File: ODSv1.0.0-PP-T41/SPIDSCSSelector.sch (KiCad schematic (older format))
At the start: 4 parts, among them U1 MAX7317, U2 74HC4067PW

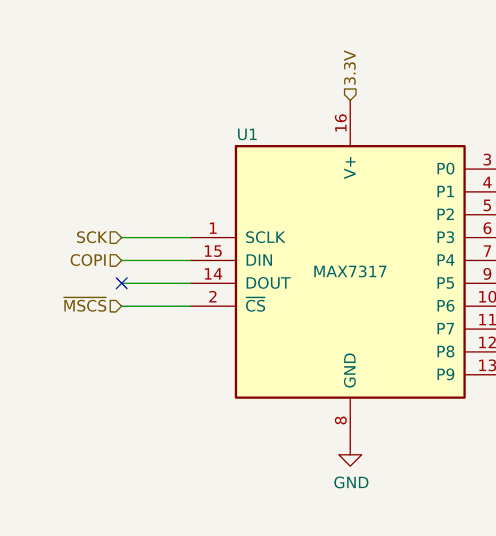
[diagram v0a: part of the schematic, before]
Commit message: Disconnect BT & BP-Jmp backbone MAX7317 DOUT (#16); make DOUT output pin
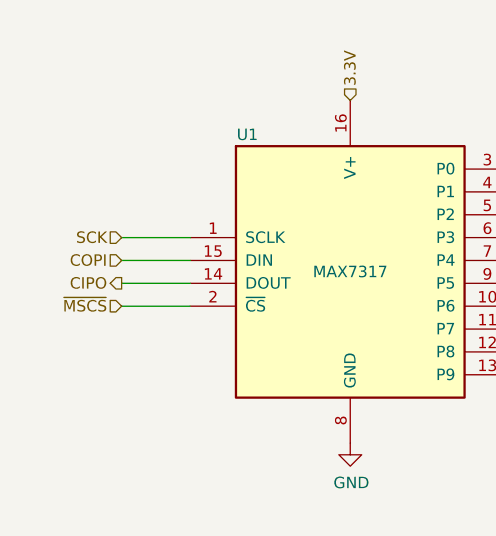
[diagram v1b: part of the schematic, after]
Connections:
- net CIPO: now reaches U1.14 (DOUT)
- no-connect marks 1 -> 0
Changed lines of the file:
@@
 	1    0    0    -1
 $EndComp
-NoConn ~ 1000 2150
+Text HLabel 1000 2150 0    50   Output ~ 0
+CIPO
 $EndSCHEMATC

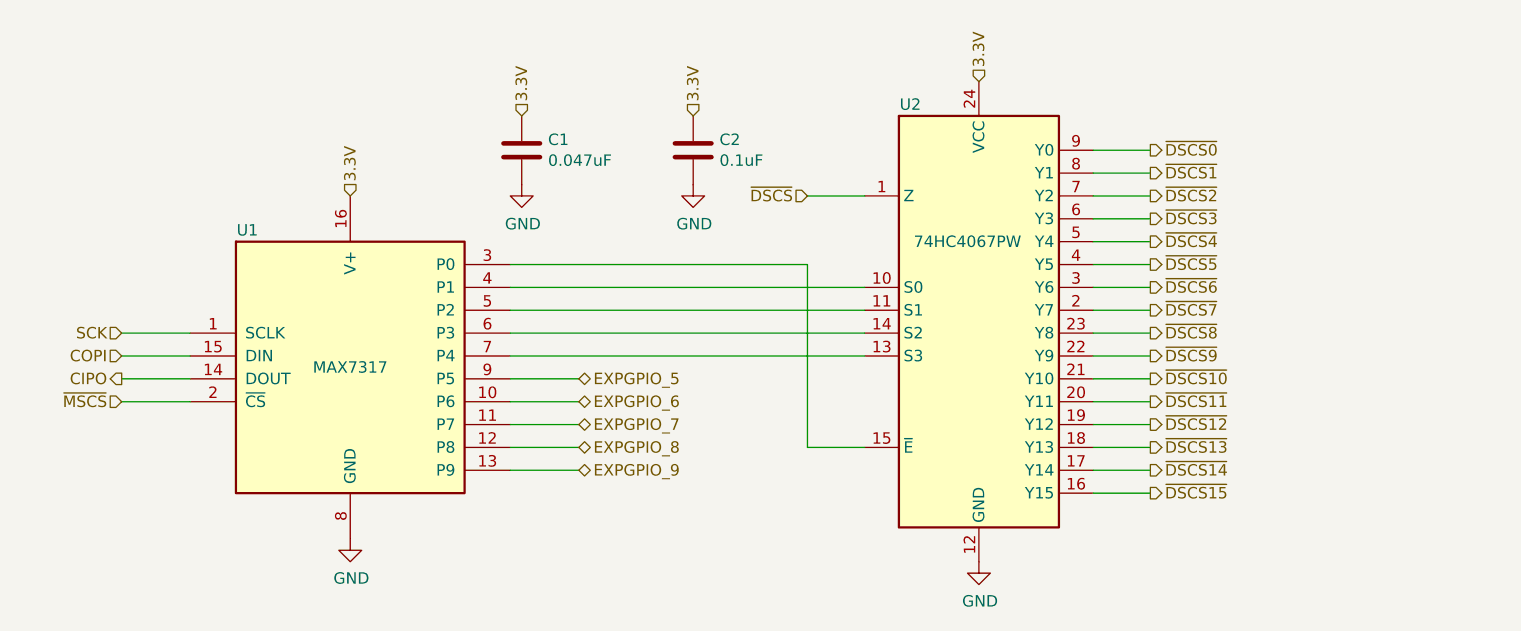
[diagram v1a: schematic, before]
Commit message: Insert 3-state buffers between all MAX7317 DOUTs and CIPO (#16)
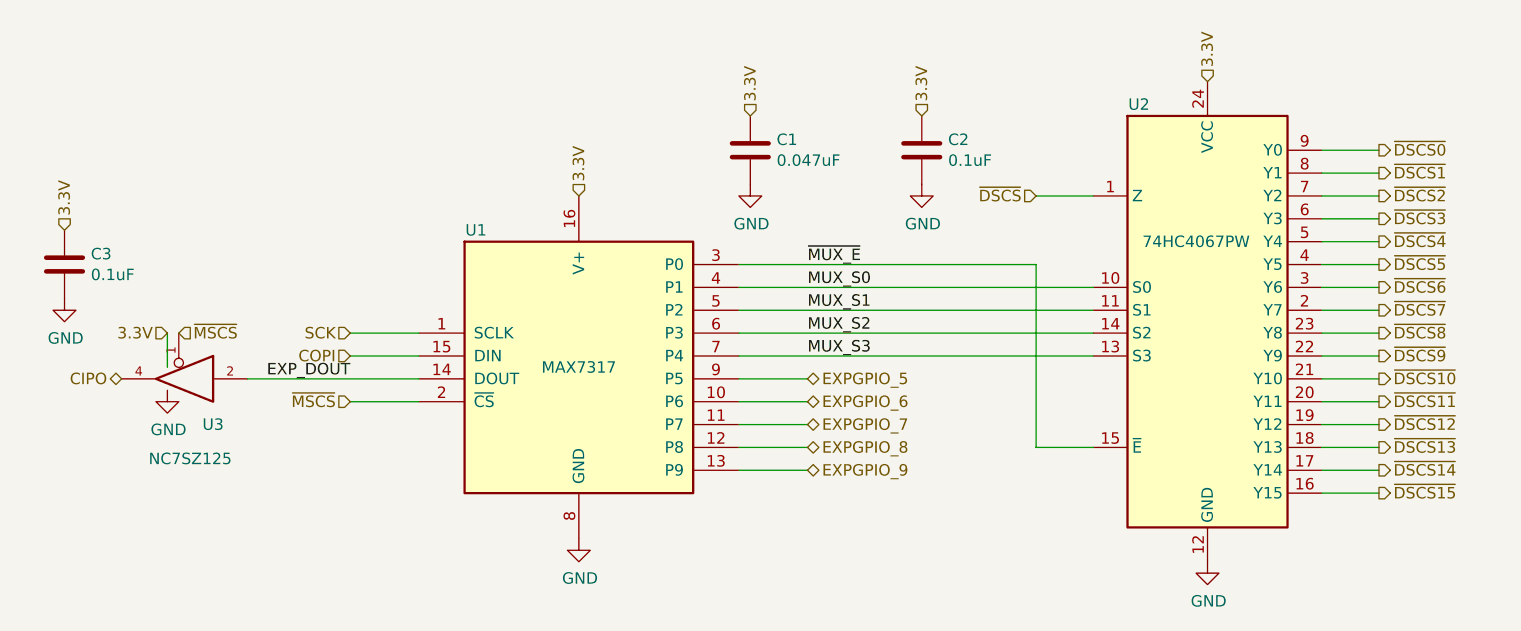
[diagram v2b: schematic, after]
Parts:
- added C3: 0.1uF, Capacitor_SMD:C_0603_1608Metric, symbol Device:C
- added U3: NC7SZ125, Package_TO_SOT_SMD:SOT-353_SC-70-5, symbol Octopi:NC7SZ125
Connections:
- net CIPO: now also U3.4; no longer U1.14 (DOUT)
- net GND: now also C3.2, U3.3 (GND)
- net ~MSCS~: now also U3.1
- net ~MUX_E~: now reaches U1.3 (P0), U2.15 (~E)
- net MUX_S0: now reaches U1.4 (P1), U2.10 (S0)
- net MUX_S1: now reaches U1.5 (P2), U2.11 (S1)
- net MUX_S2: now reaches U1.6 (P3), U2.14 (S2)
- net MUX_S3: now reaches U1.7 (P4), U2.13 (S3)
- net 3.3V renamed VCC
- net VCC: now also C3.1, U3.5 (VCC)
- new net EXP_DOUT: U1.14 (DOUT), U3.2
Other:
- moved on the sheet: C1, C2, U1, U2
